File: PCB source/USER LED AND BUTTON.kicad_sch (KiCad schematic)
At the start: 7 parts

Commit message: Pass ERC
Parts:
- added C16, C60: 100nF, PCM_JLCPCB:C_0402, symbol PCM_JLCPCB-Capacitors:0402,100nF,(2)
- added R37, R8: 100Ω, PCM_JLCPCB:R_0402, symbol PCM_JLCPCB-Resistors:0402,100Ω
- added R38, R39: 10kΩ, PCM_JLCPCB:R_0402, symbol PCM_JLCPCB-Resistors:0402,10kΩ
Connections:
- net GND: now also BTN1.1, BTN1.2, C16.2, C60.2
- net ON OFF BTN: now also C16.1, R37.2, R39.2; no longer BTN1.4
- net USER BUTTON: now also C60.1, R38.2, R8.2; no longer BTN1.3
- net +5V renamed +3V3
- net +3V3: now also R38.1, R39.1
- new net: BTN1.4, R37.1
- new net: BTN1.3, R8.1
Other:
- moved on the sheet: BTN1A, BTN1B, LED1A, LED1B, LED2A, LED2B, R33, R34, R35, R5

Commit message: Do buck Layout
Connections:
- net +3V3: no longer LED1.3
- new net +5V: LED1.3
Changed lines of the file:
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@@
-	)
-	(symbol
-		(lib_id "power:+3V3")
-		(at 59.69 69.85 0)
-		(unit 1)
-		(exclude_from_sim no)
-		(in_bom yes)
-		(on_board yes)
-		(dnp no)
-		(fields_autoplaced yes)
-		(property "Reference" "#PWR048"
-			(at 59.69 73.66 0)
-			(effects
-				(font
-					(size 1.27 1.27)
-				)
-				(hide yes)
-			)
-		)
-		(property "Value" "+3V3"
-			(at 59.69 64.77 0)
-			(effects
-				(font
-					(size 1.27 1.27)
-				)
-			)
-		)
-		(property "Footprint" ""
-			(at 59.69 69.85 0)
-			(effects
-				(font
-					(size 1.27 1.27)
-				)
-				(hide yes)
-			)
-		)
-		(property "Datasheet" ""
-			(at 59.69 69.85 0)
-			(effects
-				(font
-					(size 1.27 1.27)
-				)
-				(hide yes)
-			)
-		)
-		(property "Description" "Power symbol creates a global label with name \"+3V3\""
-			(at 59.69 69.85 0)
-			(effects
-				(font
-					(size 1.27 1.27)
-				)
-				(hide yes)
-			)
-		)
-		(pin "1"
-		)
-		(instances
-			(project ""
-				(path "/3103c9de-f1ba-4d51-8bfc-798df1c75e2f/4d4eff6e-f620-4899-aa56-71482e8e558f"
-					(reference "#PWR048")
-					(unit 1)
-				)
-			)
-		)
 	)
 	(symbol
@@
 					(unit 1)
 				)
+			)
+		)
+	)
+	(symbol
+		(lib_id "power:+5V")
+		(at 59.69 69.85 0)
+		(unit 1)
+		(exclude_from_sim no)
+		(in_bom yes)
+		(on_board yes)
+		(dnp no)
+		(fields_autoplaced yes)
+		(property "Reference" "#PWR025"
+			(at 59.69 73.66 0)
+			(effects
+				(font
+					(size 1.27 1.27)
+				)
+				(hide yes)
+			)
+		)
+		(property "Value" "+5V"
+			(at 59.69 64.77 0)
+			(effects
+				(font
+					(size 1.27 1.27)
+				)
+			)
+		)
+		(property "Footprint" ""
+			(at 59.69 69.85 0)
+			(effects
+				(font
+					(size 1.27 1.27)
+				)
+				(hide yes)
+			)
+		)
+		(property "Datasheet" ""
+			(at 59.69 69.85 0)
+			(effects
+				(font
+					(size 1.27 1.27)
+				)
+				(hide yes)
+			)
+		)
+		(property "Description" "Power symbol creates a global label with name \"+5V\""
+			(at 59.69 69.85 0)
+			(effects
+				(font
+					(size 1.27 1.27)
+				)
+				(hide yes)
+			)
+		)
+		(pin "1"
+		)
+		(instances
+			(project ""
+				(path "/3103c9de-f1ba-4d51-8bfc-798df1c75e2f/4d4eff6e-f620-4899-aa56-71482e8e558f"
+					(reference "#PWR025")
+					(unit 1)
+				)

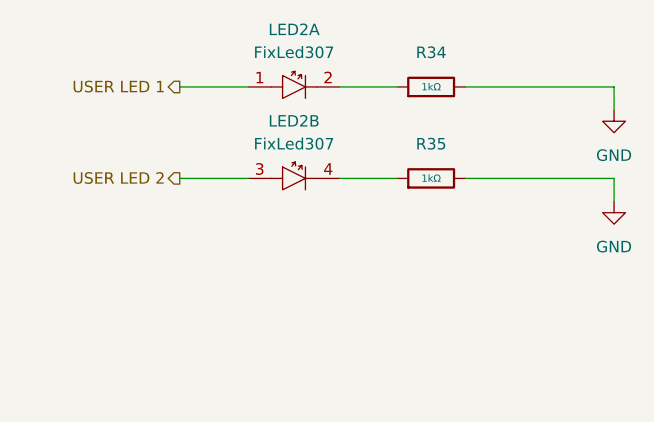
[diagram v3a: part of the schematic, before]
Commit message: Create v1 floorplan
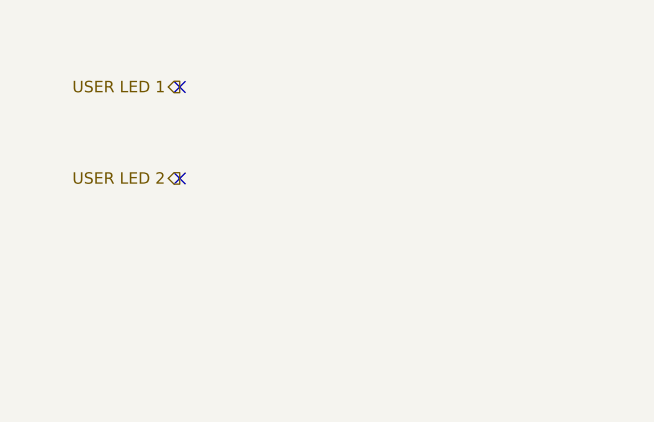
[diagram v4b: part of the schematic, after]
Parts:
- removed LED2: FixLed307, FixLed307:FixLed307, symbol FixLed307:FixLed307
- removed R34, R35: 1kΩ, PCM_JLCPCB:R_0402, symbol PCM_JLCPCB-Resistors:0402,1kΩ
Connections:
- no-connect marks 0 -> 2

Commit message: Finish layout
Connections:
- net +5V is gone; now on net +3V3: LED1.3
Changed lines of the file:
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@@
 	(wire
 		(pts
-			(xy 59.69 69.85) (xy 78.74 69.85)
+			(xy 66.04 69.85) (xy 78.74 69.85)
 		)
 		(stroke
@@
 	)
 	(symbol
+		(lib_id "power:+3V3")
+		(at 66.04 69.85 90)
+		(unit 1)
+		(exclude_from_sim no)
+		(in_bom yes)
+		(on_board yes)
+		(dnp no)
+		(fields_autoplaced yes)
+		(property "Reference" "#PWR019"
+			(at 69.85 69.85 0)
+			(effects
+				(font
+					(size 1.27 1.27)
+				)
+				(hide yes)
+			)
+		)
+		(property "Value" "+3V3"
+			(at 62.23 69.85 90)
+			(effects
+				(font
+					(size 1.27 1.27)
+				)
+				(justify left)
+			)
+		)
+		(property "Footprint" ""
+			(at 66.04 69.85 0)
+			(effects
+				(font
+					(size 1.27 1.27)
+				)
+				(hide yes)
+			)
+		)
+		(property "Datasheet" ""
+			(at 66.04 69.85 0)
+			(effects
+				(font
+					(size 1.27 1.27)
+				)
+				(hide yes)
+			)
+		)
+		(property "Description" "Power symbol creates a global label with name \"+3V3\""
+			(at 66.04 69.85 0)
+			(effects
+				(font
+					(size 1.27 1.27)
+				)
+				(hide yes)
+			)
+		)
+		(pin "1"
+		)
+		(instances
+			(project ""
+				(path "/3103c9de-f1ba-4d51-8bfc-798df1c75e2f/4d4eff6e-f620-4899-aa56-71482e8e558f"
+					(reference "#PWR019")
+					(unit 1)
+				)
+			)
+		)
+	)
+	(symbol
 		(lib_id "PCM_JLCPCB-Capacitors:0402,100nF,(2)")
 		(at 134.62 133.35 0)
@@
 					(unit 1)
 				)
-			)
-		)
-	)
-	(symbol
-		(lib_id "power:+5V")
-		(at 59.69 69.85 0)
-		(unit 1)
-		(exclude_from_sim no)
-		(in_bom yes)
-		(on_board yes)
-		(dnp no)
-		(fields_autoplaced yes)
-		(property "Reference" "#PWR025"
-			(at 59.69 73.66 0)
-			(effects
-				(font
-					(size 1.27 1.27)
-				)
-				(hide yes)
-			)
-		)
-		(property "Value" "+5V"
-			(at 59.69 64.77 0)
-			(effects
-				(font
-					(size 1.27 1.27)
-				)
-			)
-		)
-		(property "Footprint" ""
-			(at 59.69 69.85 0)
-			(effects
-				(font
-					(size 1.27 1.27)
-				)
-				(hide yes)
-			)
-		)
-		(property "Datasheet" ""
-			(at 59.69 69.85 0)
-			(effects
-				(font
-					(size 1.27 1.27)
-				)
-				(hide yes)
-			)
-		)
-		(property "Description" "Power symbol creates a global label with name \"+5V\""
-			(at 59.69 69.85 0)
-			(effects
-				(font
-					(size 1.27 1.27)
-				)
-				(hide yes)
-			)
-		)
-		(pin "1"
-		)
-		(instances
-			(project ""
-				(path "/3103c9de-f1ba-4d51-8bfc-798df1c75e2f/4d4eff6e-f620-4899-aa56-71482e8e558f"
-					(reference "#PWR025")
-					(unit 1)
-				)

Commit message: Fix schematic
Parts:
- C16, C60: Stock 5358037 -> 5436546
- R33, R5: Stock 10672962 -> 7947916
- R37, R8: Stock 2711955 -> 3389382
- R38, R39: Stock 6666349 -> 13746052
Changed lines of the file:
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@@
 (kicad_sch
-	(version 20231120)
+	(version 20250114)
 	(generator "eeschema")
-	(generator_version "8.0")
+	(generator_version "9.0")
 	(paper "A4")
 	(title_block
@@
 		(shape input)
 		(at 91.44 125.73 0)
-		(fields_autoplaced yes)
 		(effects
 			(font
@@
 		(shape output)
 		(at 146.05 69.85 180)
-		(fields_autoplaced yes)
 		(effects
 			(font
@@
 		(shape input)
 		(at 148.59 125.73 0)
-		(fields_autoplaced yes)
 		(effects
 			(font
@@
 		(shape output)
 		(at 146.05 59.69 180)
-		(fields_autoplaced yes)
 		(effects
 			(font
@@
 		(shape output)
 		(at 69.85 59.69 180)
-		(fields_autoplaced yes)
 		(effects
 			(font
@@
 			)
 		)
-		(property "Stock" "2711955"
+		(property "Stock" "3389382"
 			(at 72.39 125.73 0)
 			(effects
@@
 			)
 		)
-		(property "Stock" "10672962"
+		(property "Stock" "7947916"
 			(at 99.06 69.85 0)
 			(effects
@@
 			)
 		)
-		(property "Stock" "2711955"
+		(property "Stock" "3389382"
 			(at 129.54 125.73 0)
 			(effects
@@
 			)
 		)
-		(property "Stock" "6666349"
+		(property "Stock" "13746052"
 			(at 134.62 116.84 0)
 			(effects
@@
 			)
 		)
-		(property "Stock" "5358037"
+		(property "Stock" "5436546"
 			(at 134.62 133.35 0)
 			(effects
@@
 			)
 		)
-		(property "Stock" "10672962"
+		(property "Stock" "7947916"
 			(at 99.06 59.69 0)
 			(effects
@@
 			)
 		)
-		(property "Stock" "6666349"
+		(property "Stock" "13746052"
 			(at 77.47 116.84 0)
 			(effects
@@
 			)
 		)
-		(property "Stock" "5358037"
+		(property "Stock" "5436546"
 			(at 77.47 132.08 0)
 			(effects
